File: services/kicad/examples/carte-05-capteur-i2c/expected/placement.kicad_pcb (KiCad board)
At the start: 2 copper layers, 26 parts, among them J1 IN_5V, J2 SWD, J3 I2C, U1 STM32F103C8T6, U2 AMS1117-3.3, U3 BME280

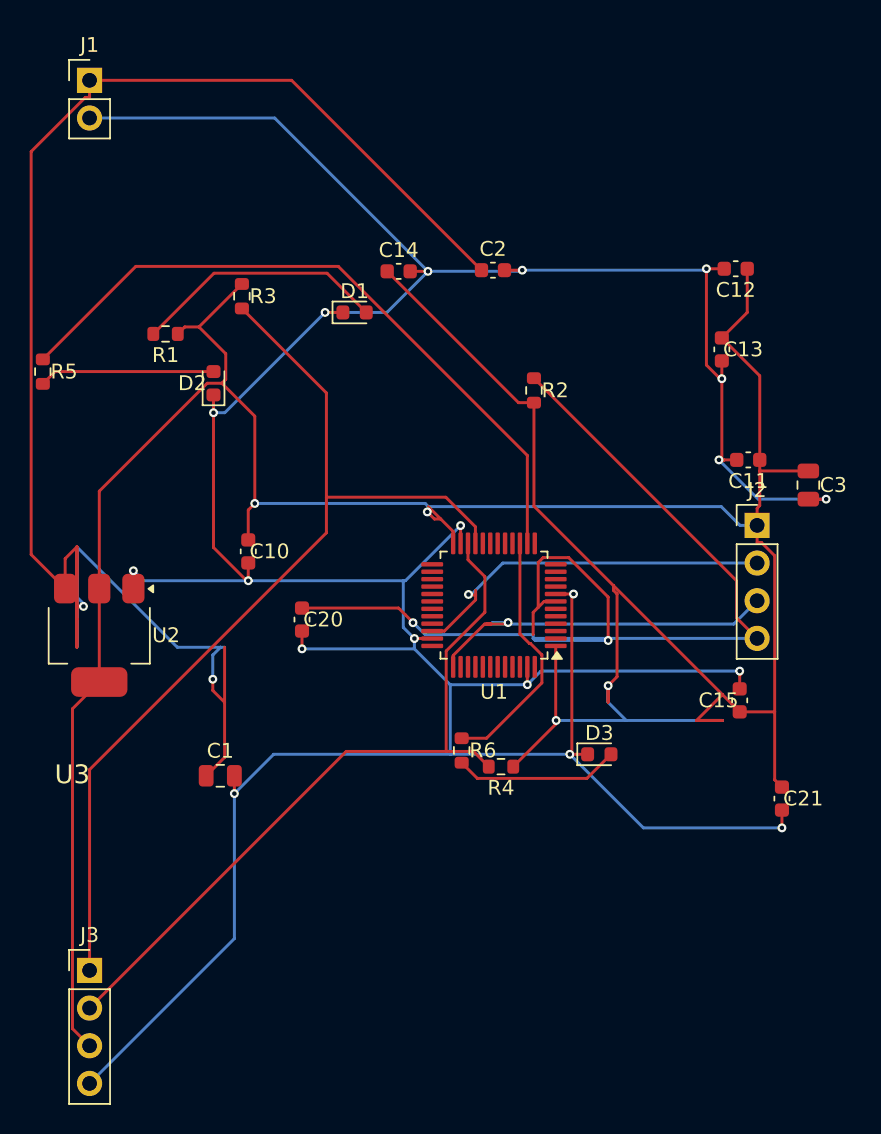
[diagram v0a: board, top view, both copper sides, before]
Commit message: test(examples): banc regenere -- placements livres, journaux et mesures a jour
- expected/placement.kicad_pcb ajoutes (carte-05, carte-06) et
  vue-dessus.png (carte-04) : le banc compare desormais le placement,
  pas seulement le board final.
- generer_exemples.py, regenerer_le_banc.py, livrer_placements.py,
  apercu_routage.py : regeneration reproductible du banc et rendus
  d apercu.
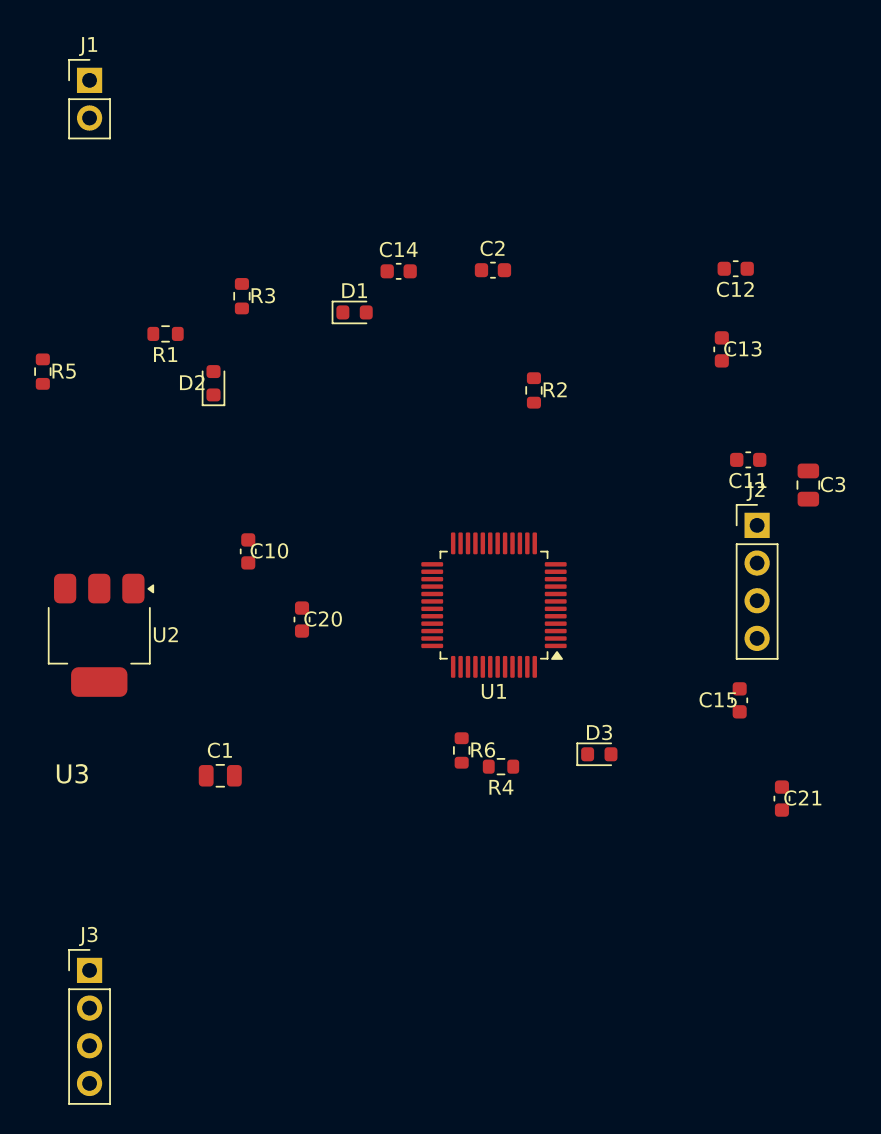
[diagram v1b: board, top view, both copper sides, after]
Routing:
- net GND: track 260.9 -> 0.00 mm, vias 19 -> 0
- net +3V3: track 237.3 -> 0.00 mm, vias 4 -> 0
- net VIN: track 127.1 -> 0.00 mm, vias 2 -> 0
- net NRST: track 75.9 -> 0.00 mm, vias 2 -> 0
- net SCL: track 65.6 -> 0.00 mm
- net SDA: track 50.1 -> 0.00 mm
- net IO_ST1: track 46.5 -> 0.00 mm
- net SWCLK: track 27.1 -> 0.00 mm, vias 1 -> 0
- net SWDIO: track 25.5 -> 0.00 mm, vias 1 -> 0
- net LED_PWR: track 17.1 -> 0.00 mm
- net IO_ST2: track 17.0 -> 0.00 mm
- net LED1_A: track 11.8 -> 0.00 mm
- net LED2_A: track 11.2 -> 0.00 mm
